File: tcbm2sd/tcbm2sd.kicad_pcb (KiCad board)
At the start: 2 copper layers, 56 x 91 mm, 27 parts, among them J1 TCBM, J2 JTAG, J4 AMS1117, J5 SD CARD, J7 ALT_A6_A7, SW1 BUT_PREV, SW2 BUT_NEXT, U1 XC9572XL-VQ64, U2 Arduino Pro Mini, U3 AMS1117-3.3, U4 27C512

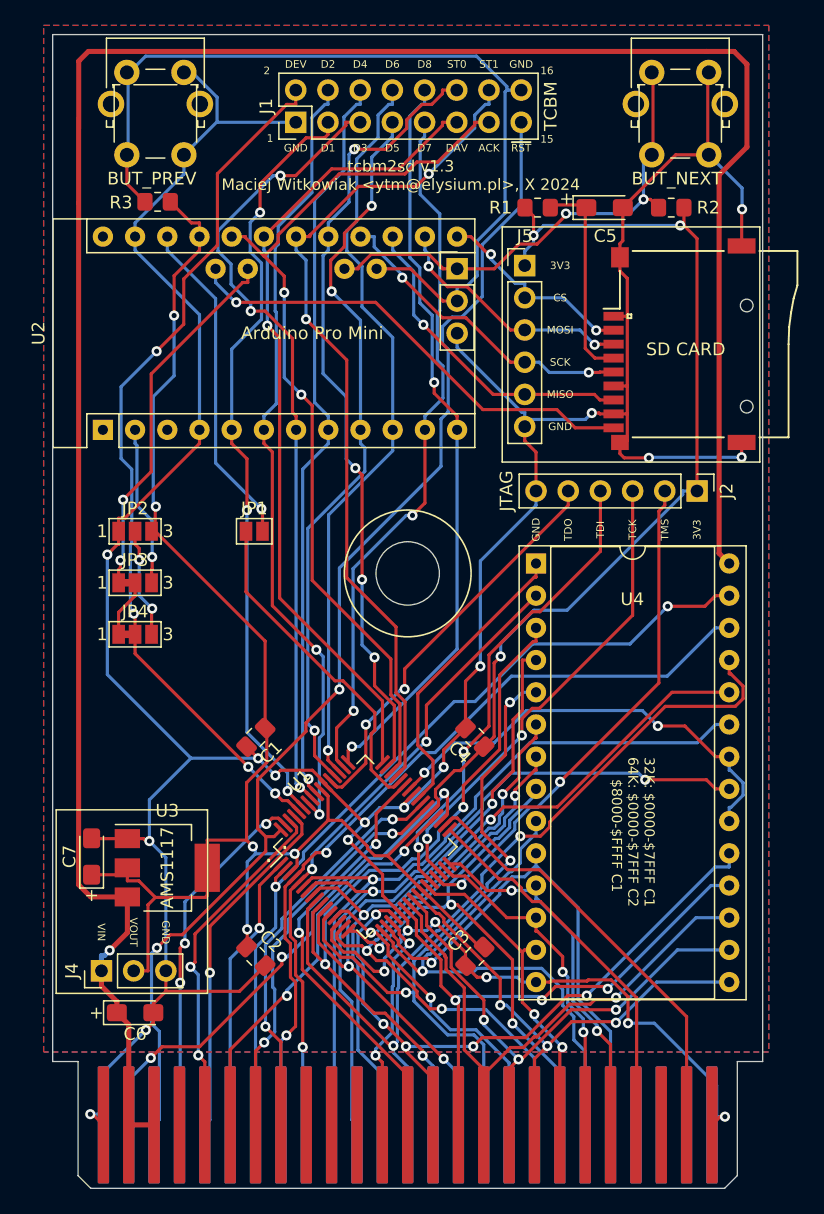
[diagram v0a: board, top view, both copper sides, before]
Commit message: Switch to 44-pin connector
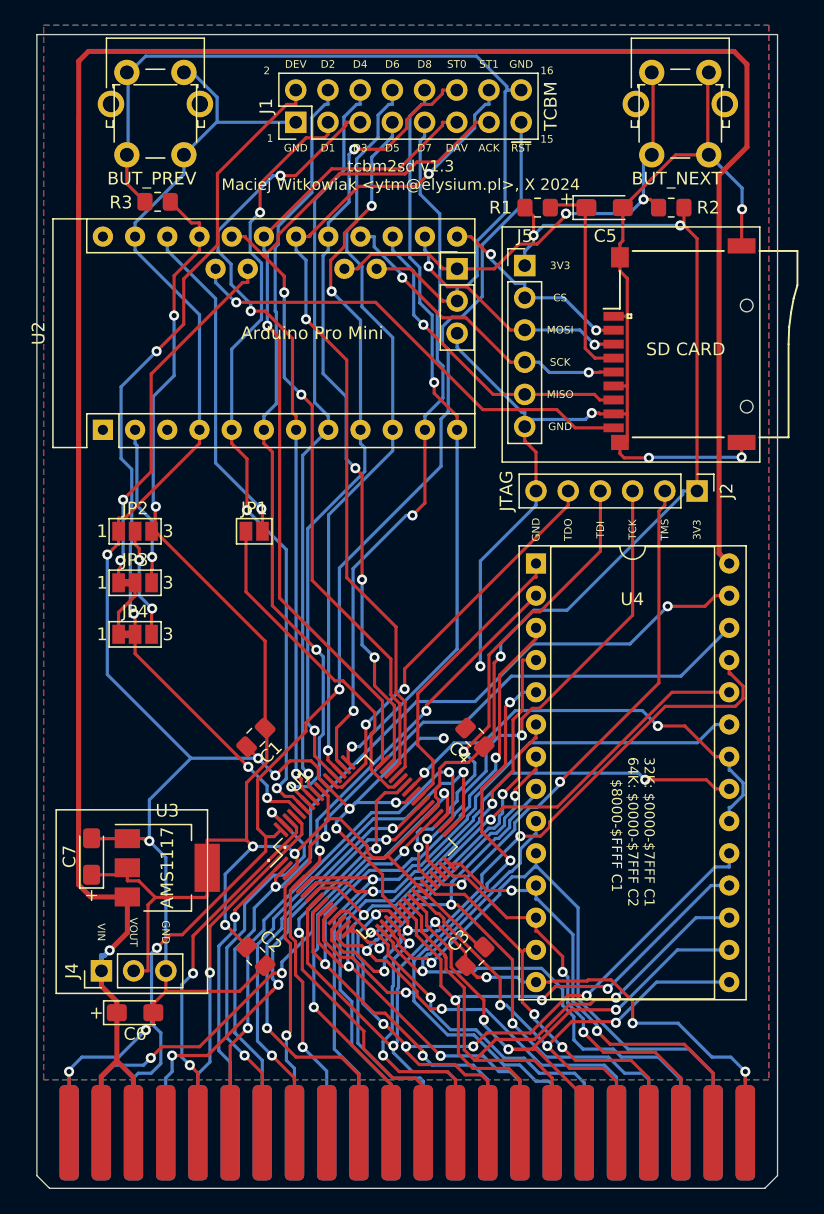
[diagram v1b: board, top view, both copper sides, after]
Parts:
- removed U$1: C16_CARTRIDGE, c264-magic-cart-rev1:C16_CART
- added U5: C16_NEWSTYLE_EXP_PORT, LittleSixteen:EdgeConn-44pin, F.Cu at (148.5, 150.4)
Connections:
- U1 pad 38: /C2LO -> /C2
- U1 pad 39: /C2HI -> /~{CS0}
- U1 pad 63: /~{RAS} -> /~{CS1}
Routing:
- net /C2: track 0.00 -> 37.5 mm, vias 0 -> 3
- net /~{CS0}: track 0.00 -> 37.4 mm, vias 0 -> 2
- net /C2HI: track 32.2 -> 0.00 mm, vias 2 -> 0
- net /~{CS1}: track 0.00 -> 32.0 mm, vias 0 -> 2
- net /C2LO: track 32.0 -> 0.00 mm, vias 2 -> 0
- net /~{RAS}: track 28.6 -> 0.00 mm, vias 3 -> 0
- net GND: track 305.2 -> 318.5 mm
- net /AEC: track 30.3 -> 43.4 mm, vias 0 -> 2
- net /A2: track 38.8 -> 50.3 mm
- net /D5: track 39.9 -> 50.2 mm
- net /A6: track 50.8 -> 59.9 mm
- net /D7: track 50.4 -> 58.9 mm
- net /D0: track 28.5 -> 35.9 mm
- net /A9: track 55.2 -> 62.4 mm
- net /BA: track 30.0 -> 36.9 mm
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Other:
- board size 56 x 91 mm -> 58.4 x 91 mm

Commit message: Retouching
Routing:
- net +3V3: track 203.3 -> 200.9 mm
- net GND: track 318.5 -> 320.0 mm
- net /R/~{W}: track 29.1 -> 28.4 mm
- net /D0: track 35.9 -> 36.6 mm, vias 2 -> 1
- net /A11: track 61.7 -> 62.3 mm
- net /A6: track 59.9 -> 59.3 mm
- net /TMS: track 40.3 -> 40.8 mm
- net /DAV: track 64.4 -> 65.0 mm
- net /D7: track 58.9 -> 58.3 mm
- net /D2: track 31.7 -> 32.3 mm
